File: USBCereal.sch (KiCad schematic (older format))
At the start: 14 parts, among them J1 USB_C, J2 Conn_01x06, U1 XC6206P332MR, U2 CH340C

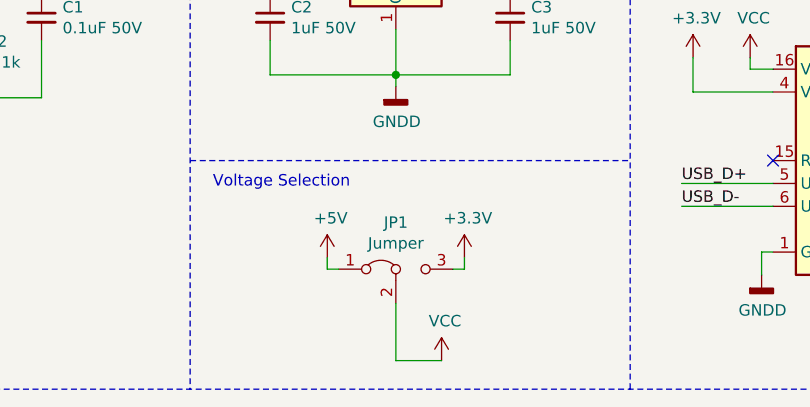
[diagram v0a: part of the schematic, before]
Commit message: Redsigned the pcb to use a switch rather than a jumper for the selection of the supply voltage
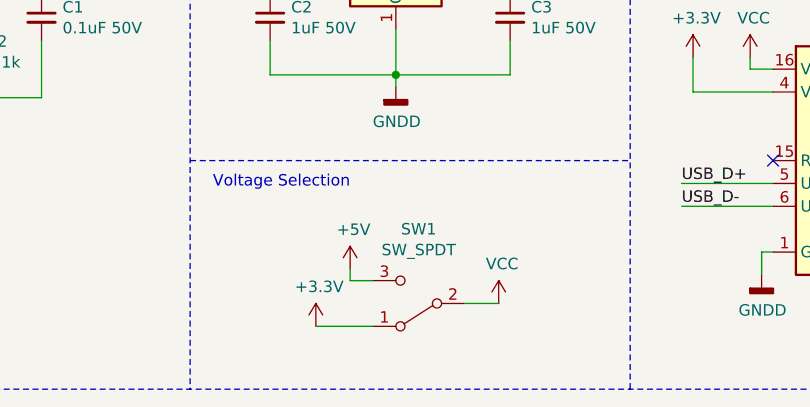
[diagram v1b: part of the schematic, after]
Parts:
- removed JP1: Jumper, Connector_PinHeader_2.54mm:PinHeader_1x03_P2.54mm_Vertical, symbol Jumper:Jumper_3_Bridged12
- added SW1: SW_SPDT, Button_Switch_SMD:SW_SPDT_CK-JS102011SAQN, symbol Switch:SW_SPDT
- C1: LCSC CL10A105KB8NNNC -> CC0603KRX7R9BB104
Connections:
- net +3V3: now also SW1.1 (A)
- net +5V: now also SW1.3 (C)
- net VCC: now also SW1.2 (B)
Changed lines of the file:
@@
 Text Label 7300 2175 2    50   ~ 0
 DTR
-$Comp
-L Jumper:Jumper_3_Bridged12 JP1
-U 1 1 60DD52A3
-P 4500 2350
-F 0 "JP1" H 4500 2554 50  0000 C CNN
-F 1 "Jumper" H 4500 2463 50  0000 C CNN
-F 2 "Connector_PinHeader_2.54mm:PinHeader_1x03_P2.54mm_Vertical" H 4500 2350 50  0001 C CNN
-F 3 "~" H 4500 2350 50  0001 C CNN
-	1    4500 2350
-	1    0    0    -1
-$EndComp
-Wire Wire Line
-	4500 2500 4500 2750
-Wire Wire Line
-	4500 2750 4700 2750
 Wire Wire Line
 	5800 1425 5800 1575
@@
 	1    0    0    -1
 $EndComp
-Wire Wire Line
-	4750 2350 4800 2350
-Wire Wire Line
-	4800 2350 4800 2300
 $Comp
 L power:+3.3V #PWR08
 U 1 1 60DE1F38
-P 4800 2300
-F 0 "#PWR08" H 4800 2150 50  0001 C CNN
-F 1 "+3.3V" H 4815 2473 50  0000 C CNN
-F 2 "" H 4800 2300 50  0001 C CNN
-F 3 "" H 4800 2300 50  0001 C CNN
-	1    4800 2300
-	1    0    0    -1
-$EndComp
-Wire Wire Line
-	4200 2350 4250 2350
-Wire Wire Line
-	4200 2300 4200 2350
+P 4150 2600
+F 0 "#PWR08" H 4150 2450 50  0001 C CNN
+F 1 "+3.3V" H 4165 2773 50  0000 C CNN
+F 2 "" H 4150 2600 50  0001 C CNN
+F 3 "" H 4150 2600 50  0001 C CNN
+	1    4150 2600
+	1    0    0    -1
+$EndComp
 $Comp
 L power:+5V #PWR05
 U 1 1 60DDFF33
-P 4200 2300
-F 0 "#PWR05" H 4200 2150 50  0001 C CNN
-F 1 "+5V" H 4215 2473 50  0000 C CNN
-F 2 "" H 4200 2300 50  0001 C CNN
-F 3 "" H 4200 2300 50  0001 C CNN
-	1    4200 2300
+P 4300 2350
+F 0 "#PWR05" H 4300 2200 50  0001 C CNN
+F 1 "+5V" H 4315 2523 50  0000 C CNN
+F 2 "" H 4300 2350 50  0001 C CNN
+F 3 "" H 4300 2350 50  0001 C CNN
+	1    4300 2350
 	1    0    0    -1
 $EndComp
@@
 L power:VCC #PWR07
 U 1 1 60DE6135
-P 4700 2750
-F 0 "#PWR07" H 4700 2600 50  0001 C CNN
-F 1 "VCC" H 4715 2923 50  0000 C CNN
-F 2 "" H 4700 2750 50  0001 C CNN
-F 3 "" H 4700 2750 50  0001 C CNN
-	1    4700 2750
+P 4950 2500
+F 0 "#PWR07" H 4950 2350 50  0001 C CNN
+F 1 "VCC" H 4965 2673 50  0000 C CNN
+F 2 "" H 4950 2500 50  0001 C CNN
+F 3 "" H 4950 2500 50  0001 C CNN
+	1    4950 2500
 	1    0    0    -1
 $EndComp
@@
 F 3 "~" H 2950 1250 50  0001 C CNN
 F 4 "CC0603KRX7R9BB104" H 2950 1250 50  0001 C CNN "Part Number"
-F 5 "CL10A105KB8NNNC" H 2950 1250 50  0001 C CNN "LCSC"
+F 5 "CC0603KRX7R9BB104" H 2950 1250 50  0001 C CNN "LCSC"
 	1    2950 1250
 	1    0    0    -1
@@
 	1    0    0    -1
 $EndComp
+$Comp
+L Switch:SW_SPDT SW1
+U 1 1 60F4623E
+P 4600 2500
+F 0 "SW1" H 4600 2175 50  0000 C CNN
+F 1 "SW_SPDT" H 4600 2266 50  0000 C CNN
+F 2 "Button_Switch_SMD:SW_SPDT_CK-JS102011SAQN" H 4600 2500 50  0001 C CNN
+F 3 "https://datasheet.lcsc.com/lcsc/1809211417_Korean-Hroparts-Elec-K3-1280S-K1_C128953.pdf" H 4600 2500 50  0001 C CNN
+F 4 "C128953" H 4600 2500 50  0001 C CNN "LCSC"
+F 5 "K3-1280S-K1" H 4600 2500 50  0001 C CNN "Part Number"
+	1    4600 2500
+	-1   0    0    1
+$EndComp
+Wire Wire Line
+	4300 2350 4300 2400
+Wire Wire Line
+	4300 2400 4400 2400
+Wire Wire Line
+	4150 2600 4400 2600
+Wire Wire Line
+	4800 2500 4950 2500
 $EndSCHEMATC
